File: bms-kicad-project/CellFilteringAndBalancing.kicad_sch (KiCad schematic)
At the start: 2 parts

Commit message: feat: added buncha shit, refer to tasks 4 and 8
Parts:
- added L1, L10, L11, L12, L13, L14, L2, L3, L4, L5, L6, L7, L8, L9: 600Ω, FixedWing:IND_BLM31PG391SN1L_MUR, symbol FixedWing:BLM31PG601SN1L
- added R10, R11, R12, R13, R14, R15, R16, R17, R18, R19, R2, R20, R21, R22, R23, R24, R25, R26, R3, R4, R5, R6, R7, R8, R9: 0, FixedWing:RC1206N_YAG, symbol FixedWing:RC1206JR-070RL
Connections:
- net C0: now also R14.2; no longer C1.1
- net C1: now also R13.2
- net C10: now also R4.2
- net C11: now also R3.2
- net C12: now also R2.2; no longer R1.2
- net C2: now also R12.2
- net C3: now also R11.2
- net C4: now also R10.2
- net C5: now also R9.2
- net C6: now also R8.2
- net C7: now also R7.2
- net C8: now also R6.2
- net C9: now also R5.2
- net Filter and Balance Cell 1/BATT(n): now also L4.2
- net Filter and Balance Cell 10/BATT(n): now also L5.1
- net Filter and Balance Cell 10/BATT(n-1): now also L7.1
- net Filter and Balance Cell 11/BATT(n): now also L3.1
- net Filter and Balance Cell 12/BATT(n): now also L1.1
- net Filter and Balance Cell 2/BATT(n): now also L6.2
- net Filter and Balance Cell 3/BATT(n): now also L8.2
- net Filter and Balance Cell 4/BATT(n): now also L10.2
- net Filter and Balance Cell 5/BATT(n): now also L12.2
- net Filter and Balance Cell 6/BATT(n): now also L13.1
- net Filter and Balance Cell 7/BATT(n): now also L11.1
- net Filter and Balance Cell 8/BATT(n): now also L9.1
- net GND: now also L2.2
- net S1: now also R26.2
- net S10: now also R17.2
- net S11: now also R16.2
- net S12: now also R15.2
- net S2: now also R25.2
- net S3: now also R24.2
- net S4: now also R23.2
- net S5: now also R22.2
- net S6: now also R21.2
- net S7: now also R20.2
- net S8: now also R19.2
- net S9: now also R18.2
- new net: L14.2, L2.1
- new net Filter and Balance Cell 1/BATT(n-1): L14.1
- new net Filter and Balance Cell 1/C(n): R13.1
- new net Filter and Balance Cell 1/C(n-1): C1.1, R14.1
- new net Filter and Balance Cell 1/S(n): R26.1
- new net Filter and Balance Cell 10/C(n): R4.1
- new net Filter and Balance Cell 10/C(n-1): R5.1
- new net Filter and Balance Cell 10/S(n): R17.1
- new net Filter and Balance Cell 11/C(n): R3.1
- new net Filter and Balance Cell 11/S(n): R16.1
- new net Filter and Balance Cell 12/C(n): R1.2, R2.1
- new net Filter and Balance Cell 12/S(n): R15.1
- new net Filter and Balance Cell 2/C(n): R12.1
- new net Filter and Balance Cell 2/S(n): R25.1
- new net Filter and Balance Cell 3/C(n): R11.1
- new net Filter and Balance Cell 3/S(n): R24.1
- new net Filter and Balance Cell 4/C(n): R10.1
- new net Filter and Balance Cell 4/S(n): R23.1
- new net Filter and Balance Cell 5/C(n): R9.1
- new net Filter and Balance Cell 5/S(n): R22.1
- new net Filter and Balance Cell 6/C(n): R8.1
- new net Filter and Balance Cell 6/S(n): R21.1
- new net Filter and Balance Cell 7/C(n): R7.1
- new net Filter and Balance Cell 7/S(n): R20.1
- new net Filter and Balance Cell 8/C(n): R6.1
- new net Filter and Balance Cell 8/S(n): R19.1
- new net Filter and Balance Cell 9/S(n): R18.1
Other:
- moved on the sheet: C1, R1

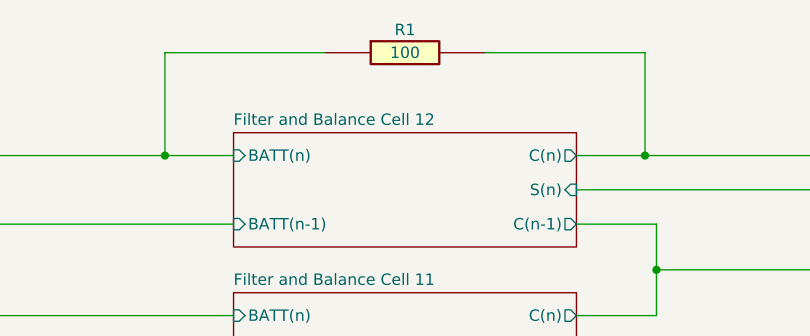
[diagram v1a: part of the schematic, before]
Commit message: feat: finished 5V reg circuit lgtm!
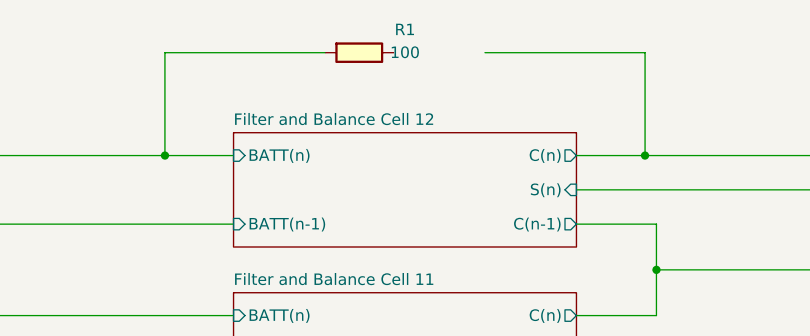
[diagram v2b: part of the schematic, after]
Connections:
- net Filter and Balance Cell 12/C(n): no longer R1.2
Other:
- moved on the sheet: R1

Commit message: feat: figured out battery stack monitor V+ biasing. Refer to task 5 on the punchlist for more details.
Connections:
- net Filter and Balance Cell 12/C(n): now also R1.2
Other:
- moved on the sheet: R1
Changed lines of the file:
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@@
     (stroke (width 0) (type default))
   )
-  (wire (pts (xy 237.49 21.59) (xy 255.27 21.59))
+  (wire (pts (xy 237.49 21.59) (xy 265.43 21.59))
     (stroke (width 0) (type default))
   )
@@
     )
   )
-  (symbol (lib_id "FixedWing:CRCW0805100RFKEA") (at 255.27 21.59 0) (unit 1)
-    (in_bom yes) (on_board yes) (dnp no)
-    (property "Reference" "R1" (at 264.16 19.05 0)
-      (effects (font (size 1.27 1.27)))
-    )
-    (property "Value" "100" (at 264.16 21.59 0)
-      (effects (font (size 1.27 1.27)))
-    )
-    (property "Footprint" "RESC2012X50N" (at 269.24 117.78 0)
-      (effects (font (size 1.27 1.27)) (justify left top) hide)
-    )
-    (property "Datasheet" "http://www.vishay.com/docs/20035/dcrcwe3.pdf" (at 269.24 217.78 0)
-      (effects (font (size 1.27 1.27)) (justify left top) hide)
-    )
-    (property "Height" "0.5" (at 269.24 417.78 0)
-      (effects (font (size 1.27 1.27)) (justify left top) hide)
-    )
-    (property "Mouser Part Number" "71-CRCW0805-100-E3" (at 269.24 517.78 0)
-      (effects (font (size 1.27 1.27)) (justify left top) hide)
-    )
-    (property "Mouser Price/Stock" "https://www.mouser.co.uk/ProductDetail/Vishay-Dale/CRCW0805100RFKEA?qs=LOX6nxTstiYDPDKmuLyNLw%3D%3D" (at 269.24 617.78 0)
-      (effects (font (size 1.27 1.27)) (justify left top) hide)
-    )
-    (property "Manufacturer_Name" "Vishay" (at 269.24 717.78 0)
-      (effects (font (size 1.27 1.27)) (justify left top) hide)
-    )
-    (property "Manufacturer_Part_Number" "CRCW0805100RFKEA" (at 269.24 817.78 0)
-      (effects (font (size 1.27 1.27)) (justify left top) hide)
-    )
+  (symbol (lib_id "FixedWing:CRCW0805100RFKEA") (at 265.43 21.59 0) (unit 1)
+    (in_bom yes) (on_board yes) (dnp no)
+    (property "Reference" "R1" (at 267.97 19.05 0)
+      (effects (font (size 1.27 1.27)))
+    )
+    (property "Value" "100" (at 269.24 21.59 0)
+      (effects (font (size 1.27 1.27)))
+    )
+    (property "Footprint" "RESC2012X50N" (at 279.4 117.78 0)
+      (effects (font (size 1.27 1.27)) (justify left top) hide)
+    )
+    (property "Datasheet" "http://www.vishay.com/docs/20035/dcrcwe3.pdf" (at 279.4 217.78 0)
+      (effects (font (size 1.27 1.27)) (justify left top) hide)
+    )
+    (property "Height" "0.5" (at 279.4 417.78 0)
+      (effects (font (size 1.27 1.27)) (justify left top) hide)
+    )
+    (property "Mouser Part Number" "71-CRCW0805-100-E3" (at 279.4 517.78 0)
+      (effects (font (size 1.27 1.27)) (justify left top) hide)
+    )
+    (property "Mouser Price/Stock" "https://www.mouser.co.uk/ProductDetail/Vishay-Dale/CRCW0805100RFKEA?qs=LOX6nxTstiYDPDKmuLyNLw%3D%3D" (at 279.4 617.78 0)
+      (effects (font (size 1.27 1.27)) (justify left top) hide)
+    )
+    (property "Manufacturer_Name" "Vishay" (at 279.4 717.78 0)
+      (effects (font (size 1.27 1.27)) (justify left top) hide)
+    )
+    (property "Manufacturer_Part_Number" "CRCW0805100RFKEA" (at 279.4 817.78 0)
+      (effects (font (size 1.27 1.27)) (justify left top) hide)
+    )

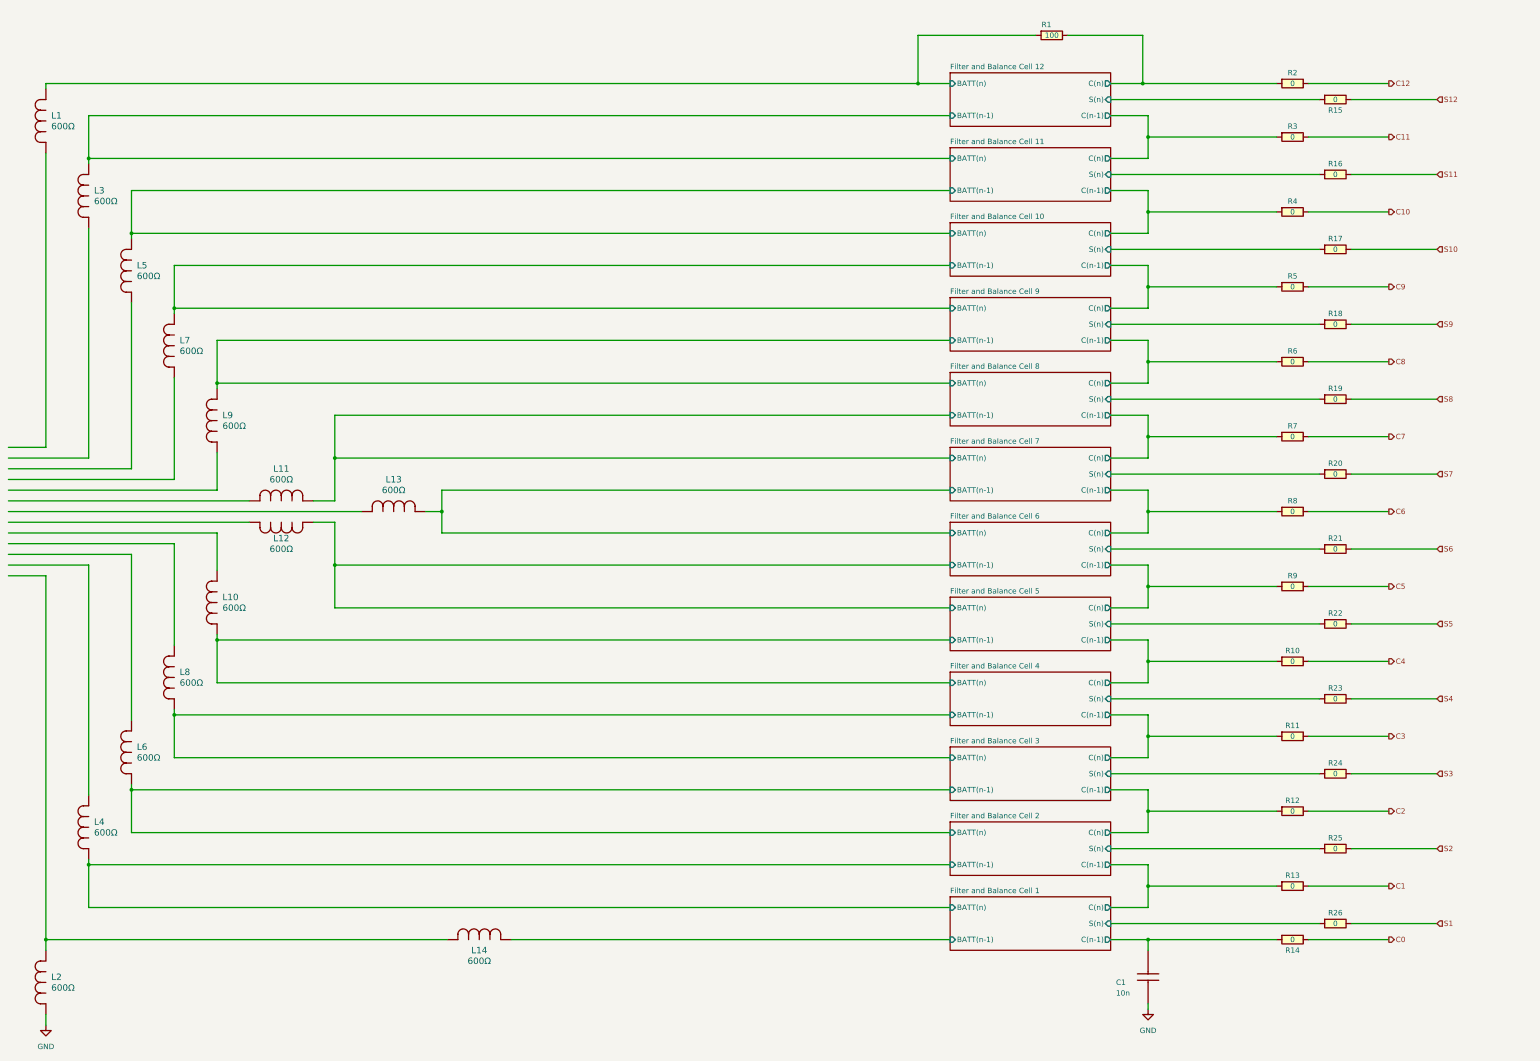
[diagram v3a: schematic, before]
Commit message: Wired up most external connections
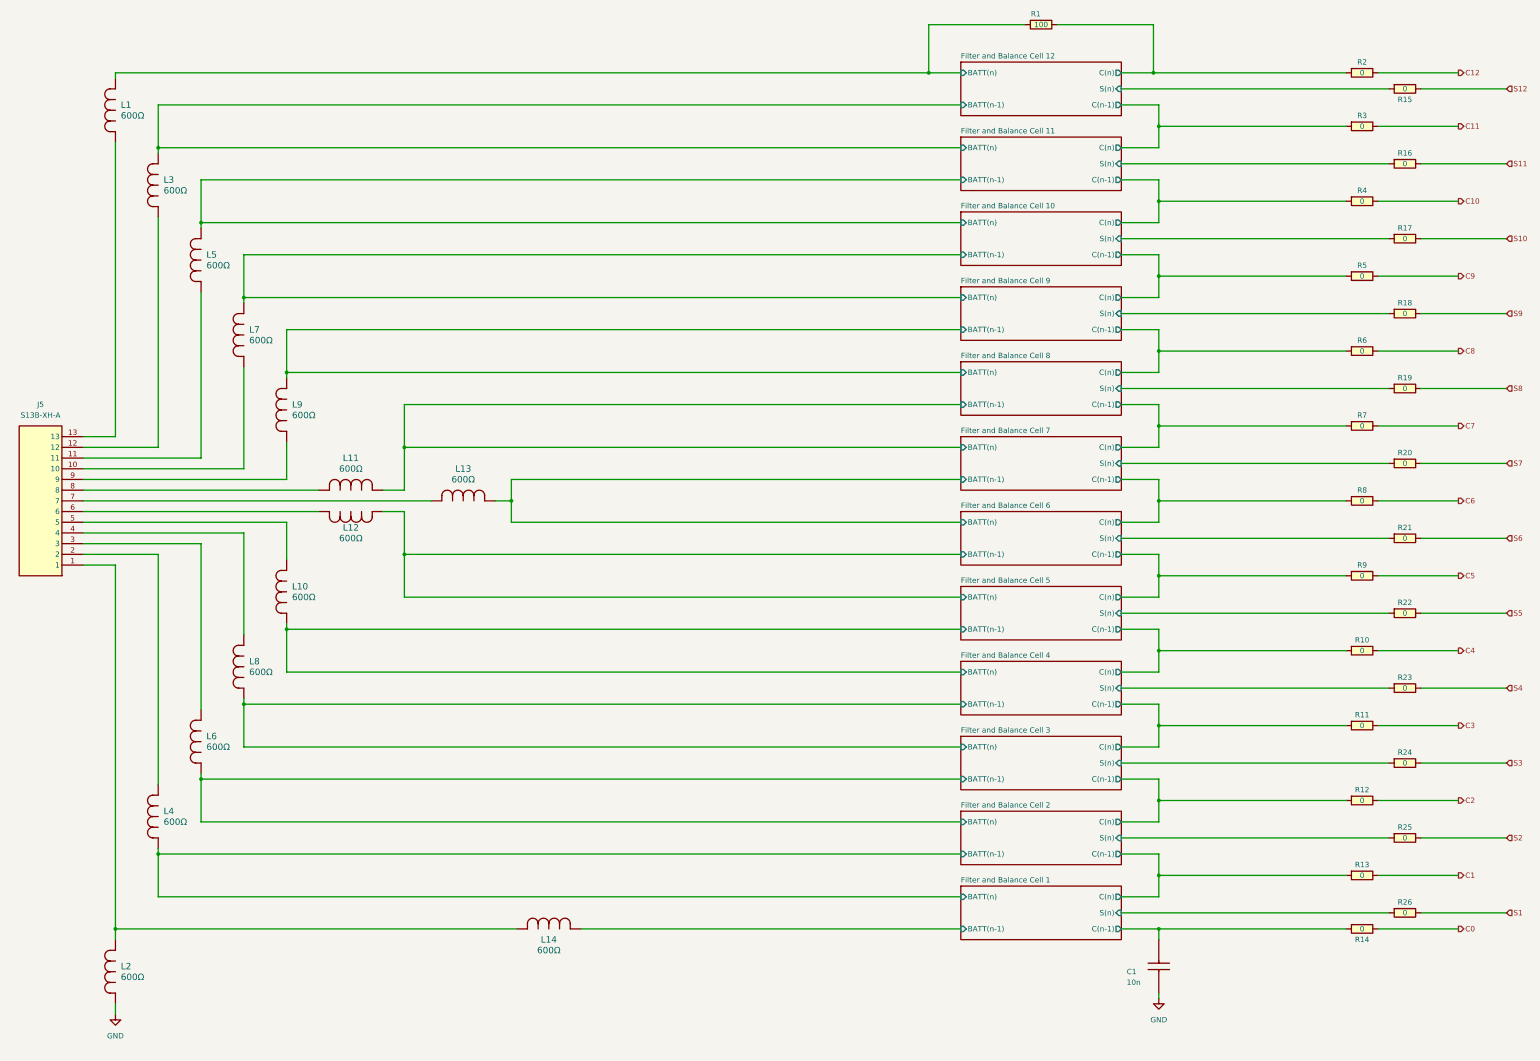
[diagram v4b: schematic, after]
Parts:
- added J5: S13B-XH-A, FixedWing:S13BXHALFSN, symbol FixedWing:S13B-XH-A
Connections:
- net at L7.2: now also J5.10
- net at L11.2: now also J5.8
- net at L14.2, L2.1: now also J5.1
- net at L9.2: now also J5.9
- net at L12.1: now also J5.6
- net at L13.2: now also J5.7
- net at L8.1: now also J5.4
- net at L6.1: now also J5.3
- net at L3.2: now also J5.12
- net at L1.2: now also J5.13
- net at L5.2: now also J5.11
- net at L4.1: now also J5.2
- net at L10.1: now also J5.5
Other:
- moved on the sheet: C1, L1, L10, L11, L12, L13, L14, L2, L3, L4, L5, L6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

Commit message: feat: Just shifting a few things around
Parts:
- renumbered J5 to J1
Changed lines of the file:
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@@
   (symbol (lib_id "power:GND") (at 46.99 254 0) (unit 1)
     (in_bom yes) (on_board yes) (dnp no) (fields_autoplaced)
-    (property "Reference" "#PWR03" (at 46.99 260.35 0)
+    (property "Reference" "#PWR01" (at 46.99 260.35 0)
       (effects (font (size 1.27 1.27)) hide)
     )
@@
       (project "bms-board"
         (path "/8a7831d1-a913-4f04-8780-225d2234b41d/95f820cc-7b9f-45ce-aa8e-ca8cb50aec5e"
-          (reference "#PWR03") (unit 1)
+          (reference "#PWR01") (unit 1)
         )
       )
@@
   (symbol (lib_id "FixedWing:S13B-XH-A") (at 39.37 147.32 180) (unit 1)
     (in_bom yes) (on_board yes) (dnp no) (fields_autoplaced)
-    (property "Reference" "J5" (at 29.21 109.22 0)
+    (property "Reference" "J1" (at 29.21 109.22 0)
       (effects (font (size 1.27 1.27)))
     )
@@
       (project "bms-board"
         (path "/8a7831d1-a913-4f04-8780-225d2234b41d/95f820cc-7b9f-45ce-aa8e-ca8cb50aec5e"
-          (reference "J5") (unit 1)
+          (reference "J1") (unit 1)
         )
       )
@@
   (symbol (lib_id "power:GND") (at 294.64 250.19 0) (unit 1)
     (in_bom yes) (on_board yes) (dnp no) (fields_autoplaced)
-    (property "Reference" "#PWR04" (at 294.64 256.54 0)
+    (property "Reference" "#PWR02" (at 294.64 256.54 0)
       (effects (font (size 1.27 1.27)) hide)
     )
@@
       (project "bms-board"
         (path "/8a7831d1-a913-4f04-8780-225d2234b41d/95f820cc-7b9f-45ce-aa8e-ca8cb50aec5e"
-          (reference "#PWR04") (unit 1)
-        )
-      )
+          (reference "#PWR02") (unit 1)
+        )
+      )

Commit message: Feature/library migration (#19)
* feat: first library migration commit

* feat: added sims directory, new cell balancing components

* feat: cell filtering/balancing switchover done

* feat: don't even know what I changed, just zoned out for several hours. Made PCB r/a mount XT-60s and solder pads into a 2-for-1 deal

* feat: schematic pretty much done

* feat: started layout

* feat: added current sense DAC

* feat: added capacitors to DAC

* feat:added more capacitors to DAC

* feat: more DAC capacitors

* feat: added temp sensor symbol/footprint

* added temp sense cad models

* feat: Added temp sensors

* feat: schematic cleanup, continued layout

* feat: added tvs protection ic to usb

* feat: placing cell filtering/balancing components

* feat: lotta layout

* feat: cell balancing board

* feat: changed cell balancing schem

* feat: slightly edited cell balance schem

* feat: big pre-design review schematic commit

* feat: post-design review clarity

* feat: I am so tired. 4-layer layout almost done

* feat: biiig layout and slight design change commit

* feat:bos->lax layout sesh

* feat: lax -> syd layout sesh

* feat: DRC run

* feat: deleted manufacturing files

* feat: silkscreen done

* feat: REV A COMMIT FOR FAB

* doc: updated schematic docs

---------

Co-authored-by: Ronan Gleason <gleason.r@northeastern.edu>
Co-authored-by: cassidysakamoto <sakamoto.ca@northeastern.edu>
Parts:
- removed C1: 10n, FixedWing:CAPC2012X95N, symbol FixedWing:AC0805KRX7R8BB103
- removed L1, L10, L11, L12, L13, L14, L2, L3, L4, L5, L6, L7, L8, L9: 600Ω, FixedWing:IND_BLM31PG391SN1L_MUR, symbol FixedWing:BLM31PG601SN1L
- removed R10, R11, R12, R13, R14, R15, R16, R17, R18, R19, R2, R20, R21, R22, R23, R24, R25, R26, R3, R4, R5, R6, R7, R8, R9: 0, FixedWing:RC1206N_YAG, symbol FixedWing:RC1206JR-070RL
- added C1, C10, C11, C12, C13, C2, C3, C4, C5, C6, C7, C8, C9: 0.1µ, FixedWing:CAP_GCJ-18_MUR, symbol FixedWing:GCJ188R72A104KA01D
- added LED1, LED10, LED11, LED12, LED2, LED3, LED4, LED5, LED6, LED7, LED8, LED9: LTST-C170KRKT, LEDC2012X120N, symbol FixedWing:LTST-C170KRKT
- added Q1, Q10, Q11, Q12, Q2, Q3, Q4, Q5, Q6, Q7, Q8, Q9: DNBT8105-7, FixedWing:SOT95P240X105-3N, symbol FixedWing:DNBT8105-7
- added R10, R15, R20, R25, R30, R35, R40, R45, R5, R50, R55, R60: 475, RESC2012X50N, symbol FixedWing:CRCW0805475RFKEA
- added R11, R16, R21, R26, R31, R36, R41, R46, R51, R56, R6, R61: 100, RESC2012X50N, symbol FixedWing:CRCW0805100RFKEA
- added R12, R17, R2, R22, R27, R32, R37, R42, R47, R52, R57, R7: 27, FixedWing:RC0805N_YAG, symbol FixedWing:RC0805FR-0727RL
- added R13, R14, R18, R19, R23, R24, R28, R29, R3, R33, R34, R38, R39, R4, R43, R44, R48, R49, R53, R54, R58, R59, R8, R9: 15, FixedWing:RES_R1632_ROM, symbol FixedWing:LTR18EZPF15R0
- added Z1, Z10, Z11, Z12, Z2, Z3, Z4, Z5, Z6, Z7, Z8, Z9: BZT52C5V6T-7, FixedWing:BZT52C5V6T7, symbol FixedWing:BZT52C5V6T-7
- R1: Manufacturer (none) -> Vishay; Manufacturer Part Number (none) -> CRCW0805100RFKEA; Manufacturer_Name Vishay -> (none); Manufacturer_Part_Number CRCW0805100RFKEA -> (none)
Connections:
- net Filter and Balance Cell 12/BATT(n) is gone; now on net GND: R1.1
- net Filter and Balance Cell 12/C(n) is gone; now on net C0: R1.2
- net C0: now also C1.2, C2.2, R2.1
- net C1: now also C2.1, C3.1, R6.2, R7.1
- net C10: now also C11.2, C12.1, R51.2, R52.1
- net C11: now also C12.2, C13.1, R56.2, R57.1
- net C12: now also C13.2, R61.2
- net C2: now also C3.2, C4.1, R11.2, R12.1
- net C3: now also C4.2, C5.1, R16.2, R17.1
- net C4: now also C5.2, C6.1, R21.2, R22.1
- net C5: now also C6.2, C7.1, R26.2, R27.1
- net C6: now also C7.2, C8.1, R31.2, R32.1
- net C7: now also C8.2, C9.1, R36.2, R37.1
- net C8: now also C10.1, C9.2, R41.2, R42.1
- net C9: now also C10.2, C11.1, R46.2, R47.1
- net GND: now also J1.1, C1.1, Q1.2 (E), Z1.2 (A)
- net at J1.10: now also Q10.2 (E), R43.2, R44.2, R45.2, R46.1, Z10.2 (A)
- net at J1.8: now also Q8.2 (E), R33.2, R34.2, R35.2, R36.1, Z8.2 (A)
- net at J1.9: now also Q9.2 (E), R38.2, R39.2, R40.2, R41.1, Z9.2 (A)
- net at J1.6: now also Q6.2 (E), R23.2, R24.2, R25.2, R26.1, Z6.2 (A)
- net at J1.7: now also Q7.2 (E), R28.2, R29.2, R30.2, R31.1, Z7.2 (A)
- net at J1.4: now also Q4.2 (E), R13.2, R14.2, R15.2, R16.1, Z4.2 (A)
- net at J1.3: now also Q3.2 (E), R10.2, R11.1, R8.2, R9.2, Z3.2 (A)
- net at J1.12: now also Q12.2 (E), R53.2, R54.2, R55.2, R56.1, Z12.2 (A)
- net at J1.13: now also R58.2, R59.2, R60.2, R61.1
- net at J1.11: now also Q11.2 (E), R48.2, R49.2, R50.2, R51.1, Z11.2 (A)
- net at J1.2: now also Q2.2 (E), R3.2, R4.2, R5.2, R6.1, Z2.2 (A)
- net at J1.5: now also Q5.2 (E), R18.2, R19.2, R20.2, R21.1, Z5.2 (A)
- new net: Q7.1 (B), R32.2, Z7.1 (K)
- new net: Q10.1 (B), R47.2, Z10.1 (K)
- new net: LED10.1 (K), Q10.3 (C), R48.1, R49.1
- new net: Q4.1 (B), R17.2, Z4.1 (K)
- new net: LED3.1 (K), Q3.3 (C), R13.1, R14.1
- new net: Q11.1 (B), R52.2, Z11.1 (K)
- new net: LED11.1 (K), Q11.3 (C), R53.1, R54.1
- new net: LED1.2 (A), R5.1
- new net: LED8.2 (A), R40.1
- new net: LED4.1 (K), Q4.3 (C), R18.1, R19.1
- new net: LED4.2 (A), R20.1
- new net: Q9.1 (B), R42.2, Z9.1 (K)
- new net: LED9.1 (K), Q9.3 (C), R43.1, R44.1
- new net: LED5.2 (A), R25.1
- new net: LED6.1 (K), Q6.3 (C), R28.1, R29.1
- new net: LED6.2 (A), R30.1
- new net: LED10.2 (A), R50.1
- new net: Q6.1 (B), R27.2, Z6.1 (K)
- new net: LED2.2 (A), R10.1
- new net: Q2.1 (B), R7.2, Z2.1 (K)
- new net: LED3.2 (A), R15.1
- new net: Q1.1 (B), R2.2, Z1.1 (K)
- new net: Q12.1 (B), R57.2, Z12.1 (K)
- new net: Q5.1 (B), R22.2, Z5.1 (K)
- new net: LED1.1 (K), Q1.3 (C), R3.1, R4.1
- new net: LED2.1 (K), Q2.3 (C), R8.1, R9.1
- new net: LED9.2 (A), R45.1
- new net: Q8.1 (B), R37.2, Z8.1 (K)
- new net: LED8.1 (K), Q8.3 (C), R38.1, R39.1
- new net: LED12.1 (K), Q12.3 (C), R58.1, R59.1
- new net: LED12.2 (A), R60.1
- new net: LED7.1 (K), Q7.3 (C), R33.1, R34.1
- new net: LED7.2 (A), R35.1
- new net: Q3.1 (B), R12.2, Z3.1 (K)
- new net: LED11.2 (A), R55.1
- new net: LED5.1 (K), Q5.3 (C), R23.1, R24.1
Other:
- removed sheet Filter and Balance Cell 1
- removed sheet Filter and Balance Cell 10
- removed sheet Filter and Balance Cell 11
- removed sheet Filter and Balance Cell 12
- removed sheet Filter and Balance Cell 2
- removed sheet Filter and Balance Cell 3
- removed sheet Filter and Balance Cell 4
- removed sheet Filter and Balance Cell 5
- removed sheet Filter and Balance Cell 6
- removed sheet Filter and Balance Cell 7
- removed sheet Filter and Balance Cell 8
- removed sheet Filter and Balance Cell 9
